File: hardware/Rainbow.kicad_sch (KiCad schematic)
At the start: 22 parts, among them J1 PICKit3, J2 UART, J3 JUMPER, J4 JACK, J5 RGB, J6 RGB, J7 RGB, J8 RGB, J9 SOURCE, Q1 Q_NMOS_GDS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

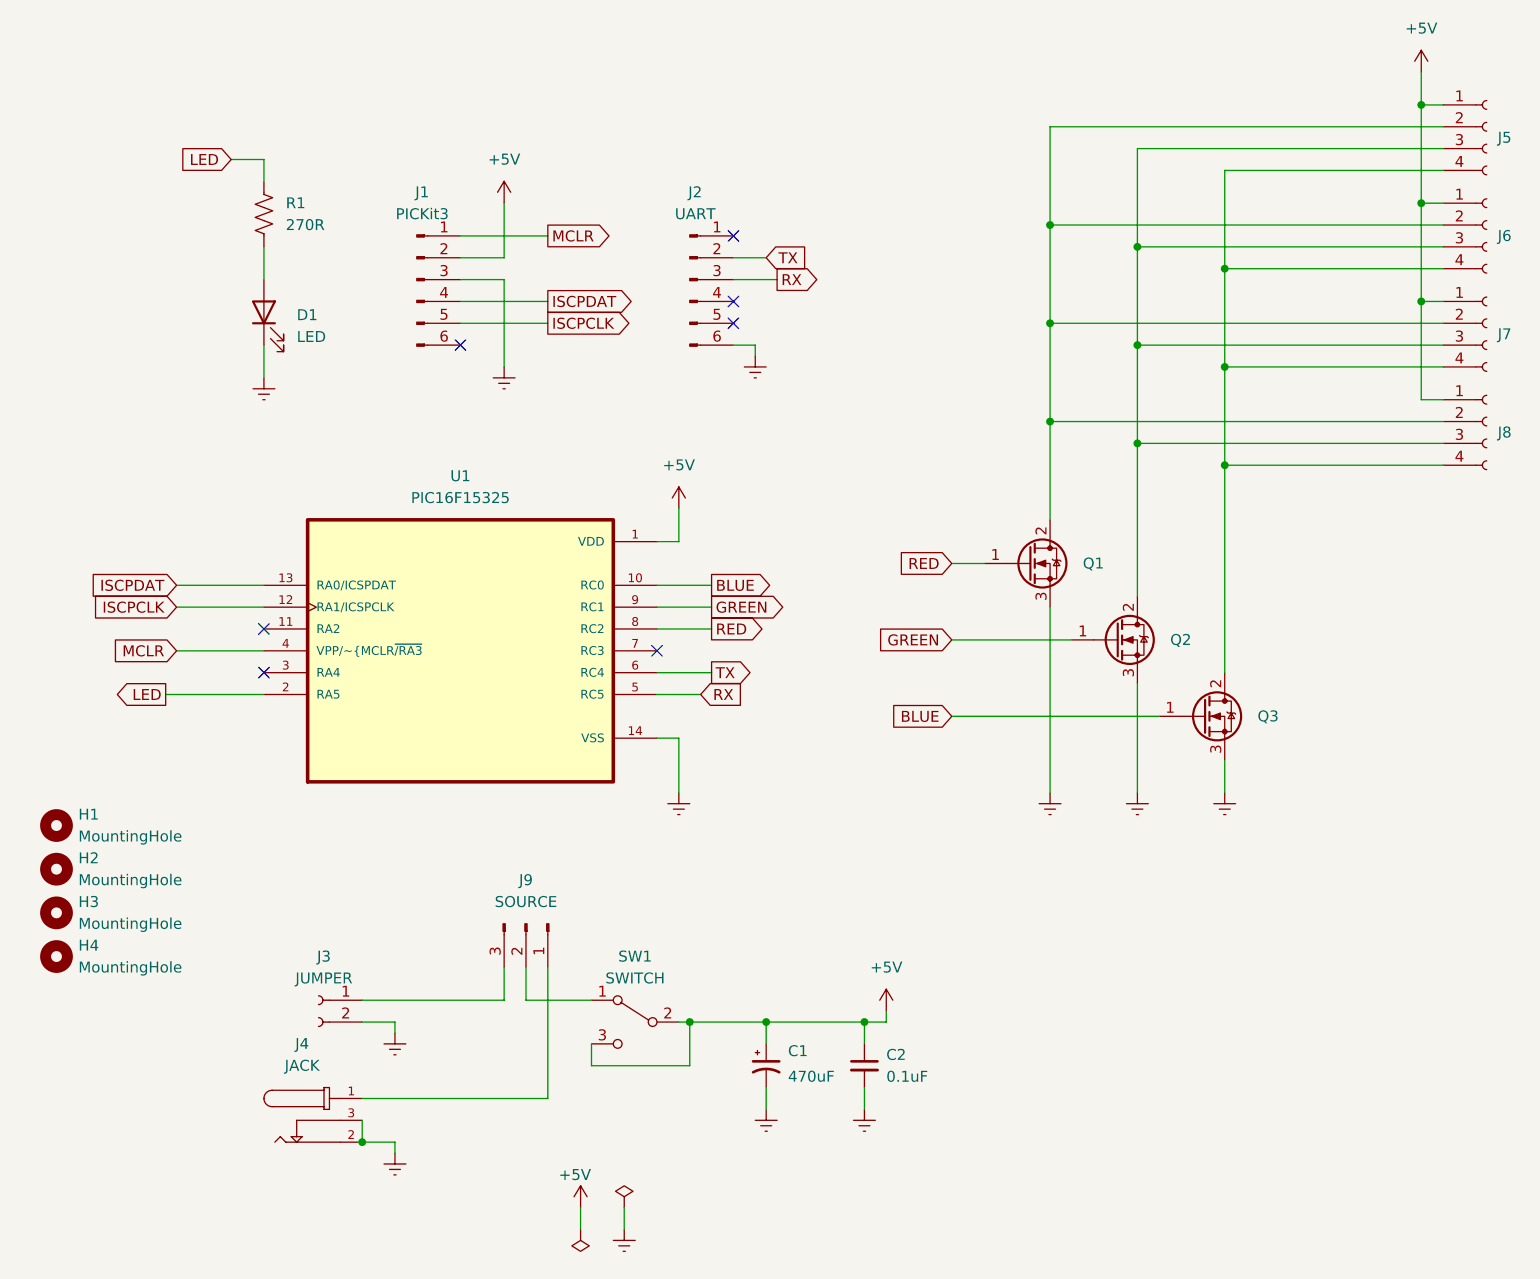
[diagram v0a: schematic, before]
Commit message: Add fuse
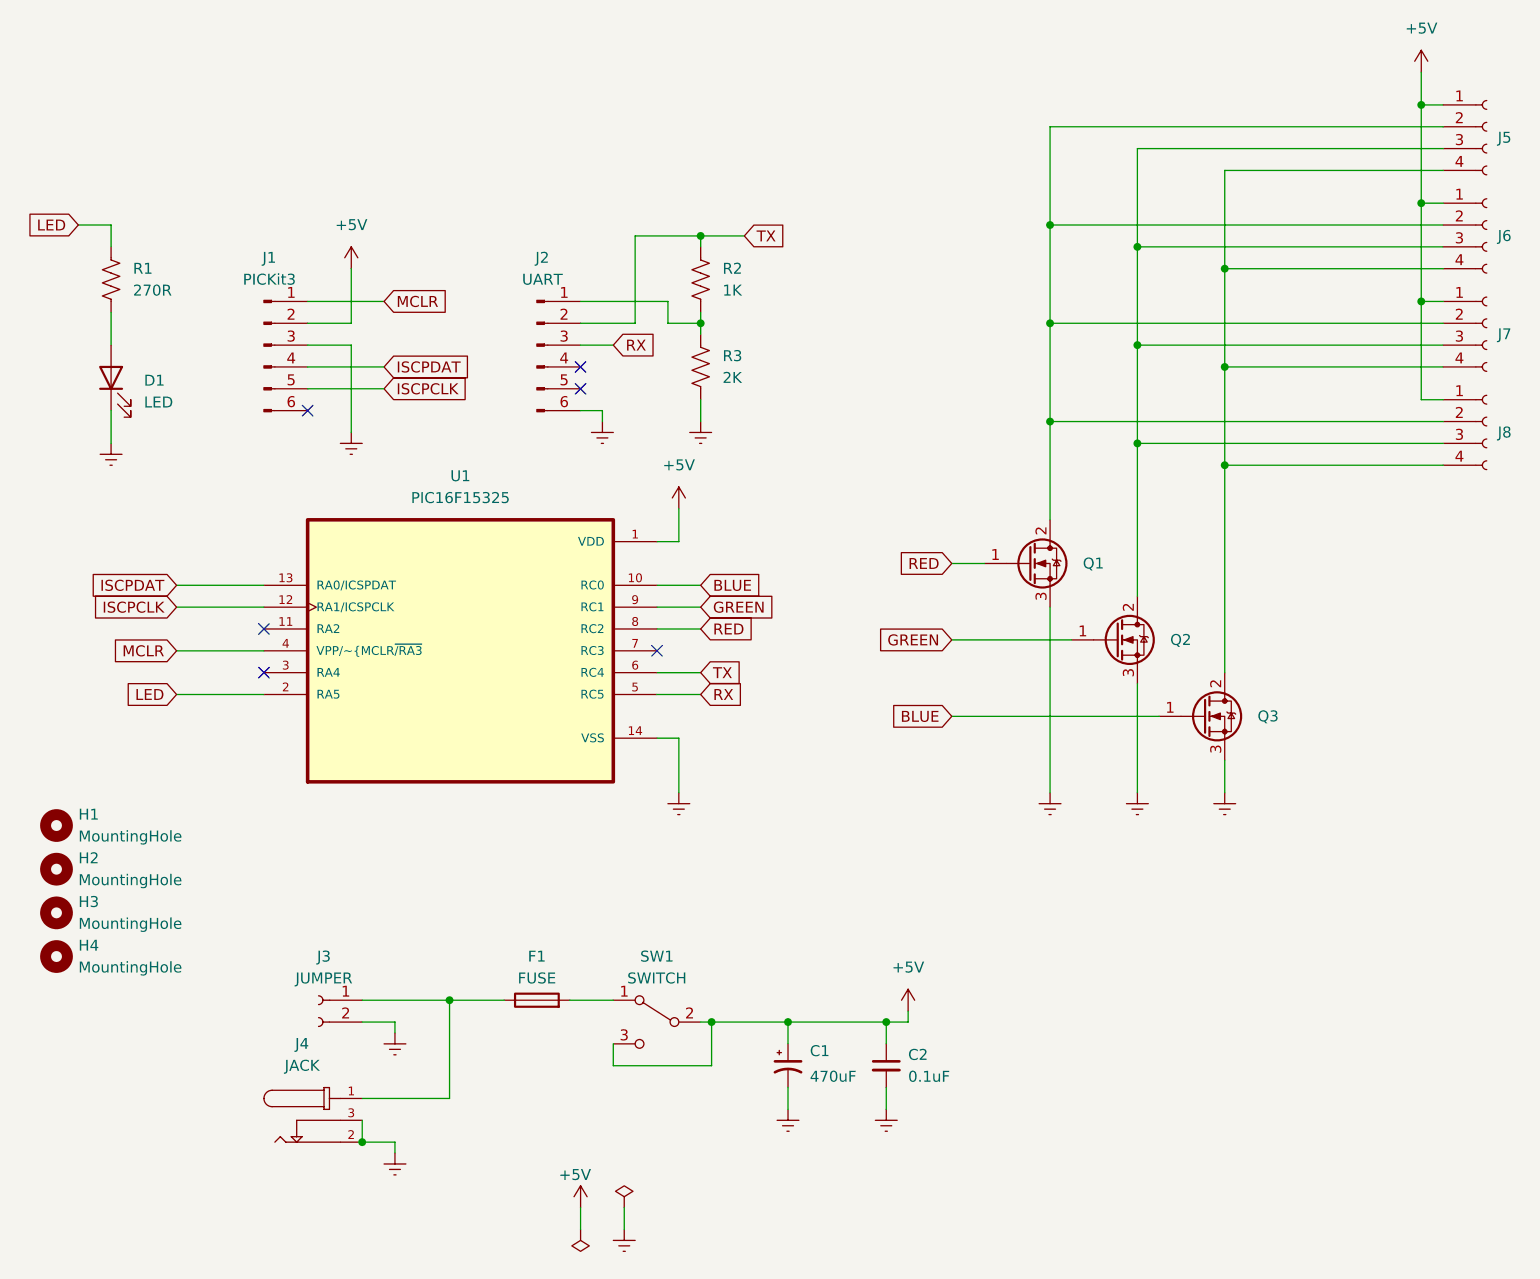
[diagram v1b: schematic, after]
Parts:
- removed J9: SOURCE, Connector_PinHeader_2.54mm:PinHeader_1x03_P2.54mm_Vertical, symbol Connector:Conn_01x03_Male
- added F1: FUSE, Fuse:Fuseholder_Blade_Mini_Keystone_3568, symbol Device:Fuse
- added R2: 1K, Resistor_THT:R_Axial_DIN0207_L6.3mm_D2.5mm_P7.62mm_Horizontal, symbol Device:R_US
- added R3: 2K, Resistor_THT:R_Axial_DIN0207_L6.3mm_D2.5mm_P7.62mm_Horizontal, symbol Device:R_US
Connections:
- net GNDREF: now also R3.2
- net TX: now also R2.1
- net at J4.1: now also J3.1 (Pin_1), F1.1
- net at J2.1 (Pin_1): now also R2.2, R3.1
- net at SW1.1 (A): now also F1.2
- no-connect marks 7 -> 6
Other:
- moved on the sheet: C1, C2, D1, J1, J2, R1, SW1

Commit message: Notes for hardware rework
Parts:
- added D2: LED, LED_THT:LED_D5.0mm, symbol Device:LED
- added R4: 270R, Resistor_THT:R_Axial_DIN0207_L6.3mm_D2.5mm_P7.62mm_Horizontal, symbol Device:R_US
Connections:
- net +5V: now also R4.1
- net GNDREF: now also D2.1 (K)
- new net: D2.2 (A), R4.2
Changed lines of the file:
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@@
   (junction (at 167.64 46.99) (diameter 0) (color 0 0 0 0)
+  )
+  (junction (at 149.86 137.16) (diameter 0) (color 0 0 0 0)
   )
   (junction (at 157.48 55.88) (diameter 0) (color 0 0 0 0)
@@
     (stroke (width 0) (type default) (color 0 0 0 0))
   )
+  (wire (pts (xy 149.86 158.75) (xy 149.86 162.56))
+    (stroke (width 0) (type default) (color 0 0 0 0))
+  )
   (wire (pts (xy 146.05 92.71) (xy 160.02 92.71))
     (stroke (width 0) (type default) (color 0 0 0 0))
@@
     (stroke (width 0) (type default) (color 0 0 0 0))
   )
-  (wire (pts (xy 140.97 135.89) (xy 140.97 137.16))
-    (stroke (width 0) (type default) (color 0 0 0 0))
-  )
   (wire (pts (xy 203.2 33.02) (xy 157.48 33.02))
     (stroke (width 0) (type default) (color 0 0 0 0))
@@
     (stroke (width 0) (type default) (color 0 0 0 0))
   )
+  (wire (pts (xy 149.86 147.32) (xy 149.86 151.13))
+    (stroke (width 0) (type default) (color 0 0 0 0))
+  )
   (wire (pts (xy 111.76 91.44) (xy 116.84 91.44))
     (stroke (width 0) (type default) (color 0 0 0 0))
@@
     (stroke (width 0) (type default) (color 0 0 0 0))
   )
+  (wire (pts (xy 138.43 137.16) (xy 149.86 137.16))
+    (stroke (width 0) (type default) (color 0 0 0 0))
+  )
   (wire (pts (xy 203.2 35.56) (xy 167.64 35.56))
     (stroke (width 0) (type default) (color 0 0 0 0))
@@
     (stroke (width 0) (type default) (color 0 0 0 0))
   )
+  (wire (pts (xy 149.86 137.16) (xy 156.21 137.16))
+    (stroke (width 0) (type default) (color 0 0 0 0))
+  )
   (wire (pts (xy 106.68 142.24) (xy 118.11 142.24))
     (stroke (width 0) (type default) (color 0 0 0 0))
@@
     (stroke (width 0) (type default) (color 0 0 0 0))
   )
+  (wire (pts (xy 156.21 135.89) (xy 156.21 137.16))
+    (stroke (width 0) (type default) (color 0 0 0 0))
+  )
   (wire (pts (xy 114.3 77.47) (xy 114.3 81.28))
     (stroke (width 0) (type default) (color 0 0 0 0))
   )
+  (wire (pts (xy 149.86 137.16) (xy 149.86 139.7))
+    (stroke (width 0) (type default) (color 0 0 0 0))
+  )
   (wire (pts (xy 77.47 134.62) (xy 87.63 134.62))
     (stroke (width 0) (type default) (color 0 0 0 0))
@@
   )
   (wire (pts (xy 76.2 55.88) (xy 76.2 49.53))
-    (stroke (width 0) (type default) (color 0 0 0 0))
-  )
-  (wire (pts (xy 140.97 137.16) (xy 138.43 137.16))
     (stroke (width 0) (type default) (color 0 0 0 0))
   )
@@
     )
     (property "Datasheet" "" (id 3) (at 76.2 68.58 0)
+      (effects (font (size 1.27 1.27)) hide)
+    )
+    (pin "1")
+  )
+  (symbol (lib_id "power:GNDREF") (at 149.86 162.56 0) (unit 1)
+    (in_bom yes) (on_board yes) (fields_autoplaced)
+    (property "Reference" "#PWR0104" (id 0) (at 149.86 168.91 0)
+      (effects (font (size 1.27 1.27)) hide)
+    )
+    (property "Value" "GNDREF" (id 1) (at 149.86 167.64 0)
+      (effects (font (size 1.27 1.27)) hide)
+    )
+    (property "Footprint" "" (id 2) (at 149.86 162.56 0)
+      (effects (font (size 1.27 1.27)) hide)
+    )
+    (property "Datasheet" "" (id 3) (at 149.86 162.56 0)
       (effects (font (size 1.27 1.27)) hide)
     )
@@
     (pin "1")
   )
-  (symbol (lib_id "power:+5V") (at 140.97 135.89 0) (mirror y) (unit 1)
-    (in_bom yes) (on_board yes) (fields_autoplaced)
-    (property "Reference" "#PWR09" (id 0) (at 140.97 139.7 0)
-      (effects (font (size 1.27 1.27)) hide)
-    )
-    (property "Value" "+5V" (id 1) (at 140.97 130.81 0))
-    (property "Footprint" "" (id 2) (at 140.97 135.89 0)
-      (effects (font (size 1.27 1.27)) hide)
-    )
-    (property "Datasheet" "" (id 3) (at 140.97 135.89 0)
+  (symbol (lib_id "power:+5V") (at 156.21 135.89 0) (mirror y) (unit 1)
+    (in_bom yes) (on_board yes)
+    (property "Reference" "#PWR09" (id 0) (at 156.21 139.7 0)
+      (effects (font (size 1.27 1.27)) hide)
+    )
+    (property "Value" "+5V" (id 1) (at 156.21 130.81 0))
+    (property "Footprint" "" (id 2) (at 156.21 135.89 0)
+      (effects (font (size 1.27 1.27)) hide)
+    )
+    (property "Datasheet" "" (id 3) (at 156.21 135.89 0)
       (effects (font (size 1.27 1.27)) hide)
     )
@@
     (pin "1")
   )
+  (symbol (lib_id "Device:LED") (at 149.86 154.94 90) (unit 1)
+    (in_bom yes) (on_board yes) (fields_autoplaced)
+    (property "Reference" "D2" (id 0) (at 153.67 155.2574 90)
+      (effects (font (size 1.27 1.27)) (justify right))
+    )
+    (property "Value" "LED" (id 1) (at 153.67 157.7974 90)
+      (effects (font (size 1.27 1.27)) (justify right))
+    )
+    (property "Footprint" "LED_THT:LED_D5.0mm" (id 2) (at 149.86 154.94 0)
+      (effects (font (size 1.27 1.27)) hide)
+    )
+    (property "Datasheet" "~" (id 3) (at 149.86 154.94 0)
+      (effects (font (size 1.27 1.27)) hide)
+    )
+    (pin "1")
+    (pin "2")
+  )
   (symbol (lib_id "Device:LED") (at 48.26 62.23 90) (unit 1)
     (in_bom yes) (on_board yes) (fields_autoplaced)
@@
     )
     (property "Datasheet" "~" (id 3) (at 48.26 62.23 0)
+      (effects (font (size 1.27 1.27)) hide)
+    )
+    (pin "1")
+    (pin "2")
+  )
+  (symbol (lib_id "Device:R_US") (at 149.86 143.51 0) (unit 1)
+    (in_bom yes) (on_board yes) (fields_autoplaced)
+    (property "Reference" "R4" (id 0) (at 152.4 142.2399 0)
+      (effects (font (size 1.27 1.27)) (justify left))
+    )
+    (property "Value" "270R" (id 1) (at 152.4 144.7799 0)
+      (effects (font (size 1.27 1.27)) (justify left))
+    )
+    (property "Footprint" "Resistor_THT:R_Axial_DIN0207_L6.3mm_D2.5mm_P7.62mm_Horizontal" (id 2) (at 150.876 143.764 90)
+      (effects (font (size 1.27 1.27)) hide)
+    )
+    (property "Datasheet" "~" (id 3) (at 149.86 143.51 0)
       (effects (font (size 1.27 1.27)) hide)
     )
@@
       (reference "#PWR0103") (unit 1) (value "+5V") (footprint "")
     )
+    (path "/8fd2453d-9dcb-42d4-be0e-4e17cf094c8a"
+      (reference "#PWR0104") (unit 1) (value "GNDREF") (footprint "")
+    )
     (path "/8ab3c0b4-3e09-4b9f-8242-15c09eeeb9e0"
       (reference "C1") (unit 1) (value "470uF") (footprint "Capacitor_THT:CP_Radial_D8.0mm_P3.50mm")
@@
       (reference "D1") (unit 1) (value "LED") (footprint "LED_THT:LED_D5.0mm")
     )
+    (path "/eb3dd94f-5032-494c-9000-b327e5febd9d"
+      (reference "D2") (unit 1) (value "LED") (footprint "LED_THT:LED_D5.0mm")
+    )
     (path "/410def68-8b62-4888-9363-5c9e7c3dbfbc"
       (reference "F1") (unit 1) (value "FUSE") (footprint "Fuse:Fuseholder_Blade_Mini_Keystone_3568")
@@
       (reference "R3") (unit 1) (value "2K") (footprint "Resistor_THT:R_Axial_DIN0207_L6.3mm_D2.5mm_P7.62mm_Horizontal")
     )
+    (path "/ed9a64cc-5a83-4784-ba3a-2dba88b6189e"
+      (reference "R4") (unit 1) (value "270R") (footprint "Resistor_THT:R_Axial_DIN0207_L6.3mm_D2.5mm_P7.62mm_Horizontal")
+    )
     (path "/c91e9575-f433-4055-8bf6-569be8c9a305"
